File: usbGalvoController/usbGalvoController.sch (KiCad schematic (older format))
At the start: 26 parts, among them P1 USB_OTG, P2 CONN_01X06, P3 GND, P4 PWR, P5 DAC, P6 GPIO, P7 UART, U1 STM32L151x6, U2 LD1117S33CTR, Y1 8MHz

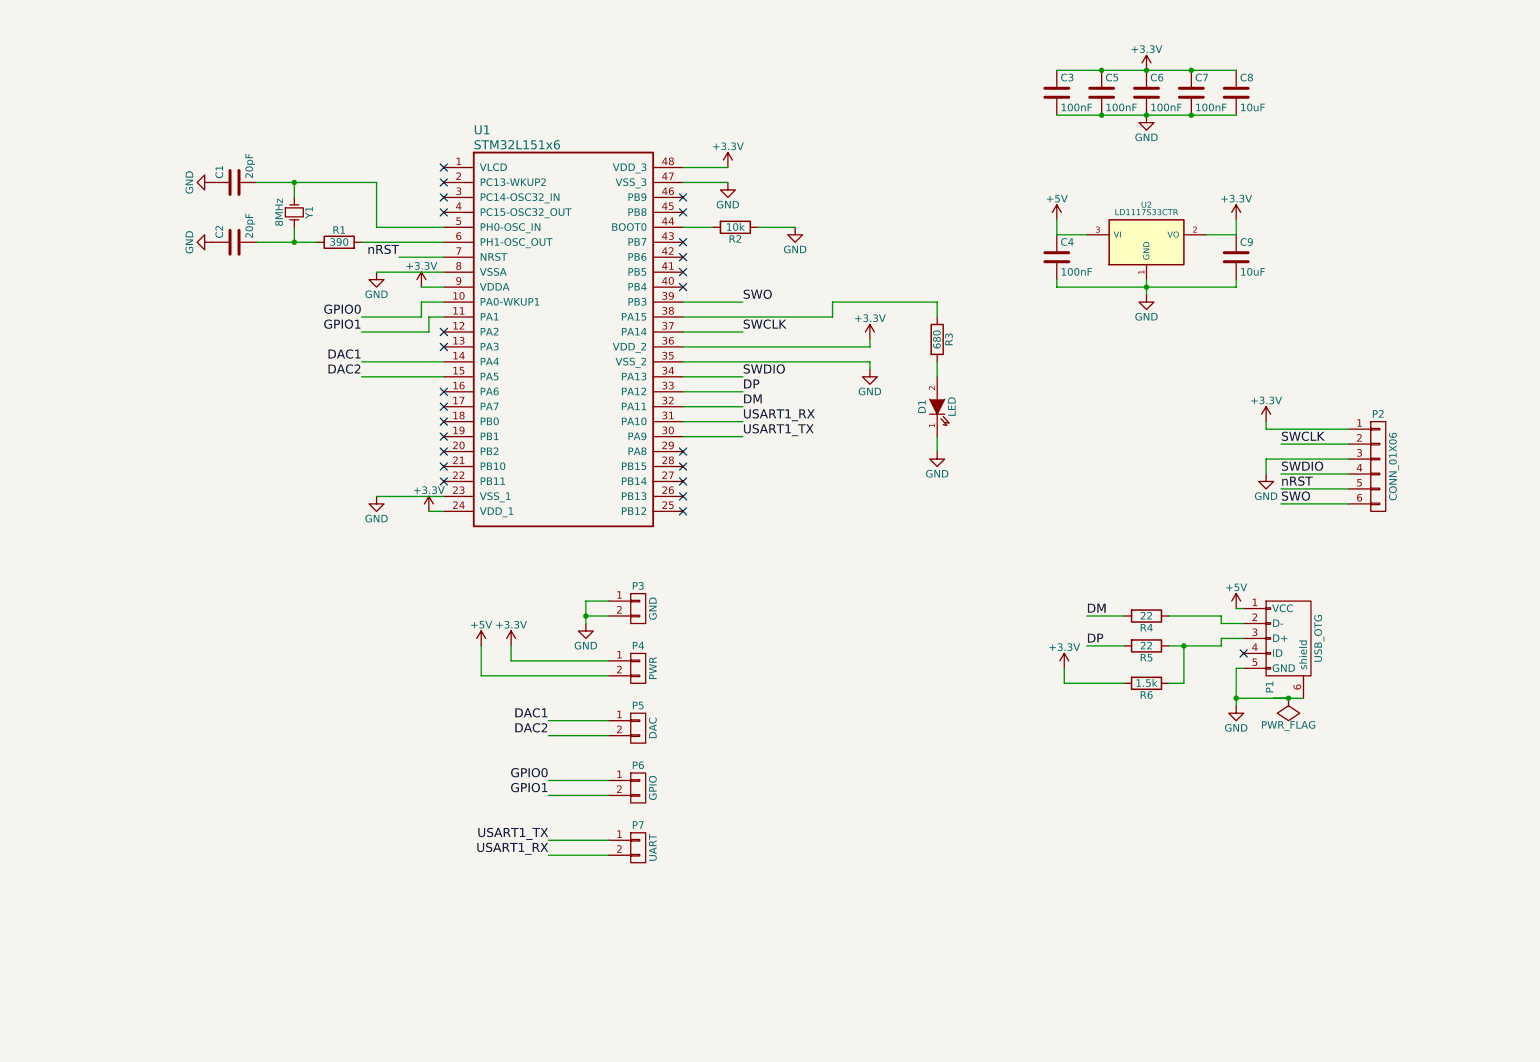
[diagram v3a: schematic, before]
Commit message: Start updating usbGalvoController schematic
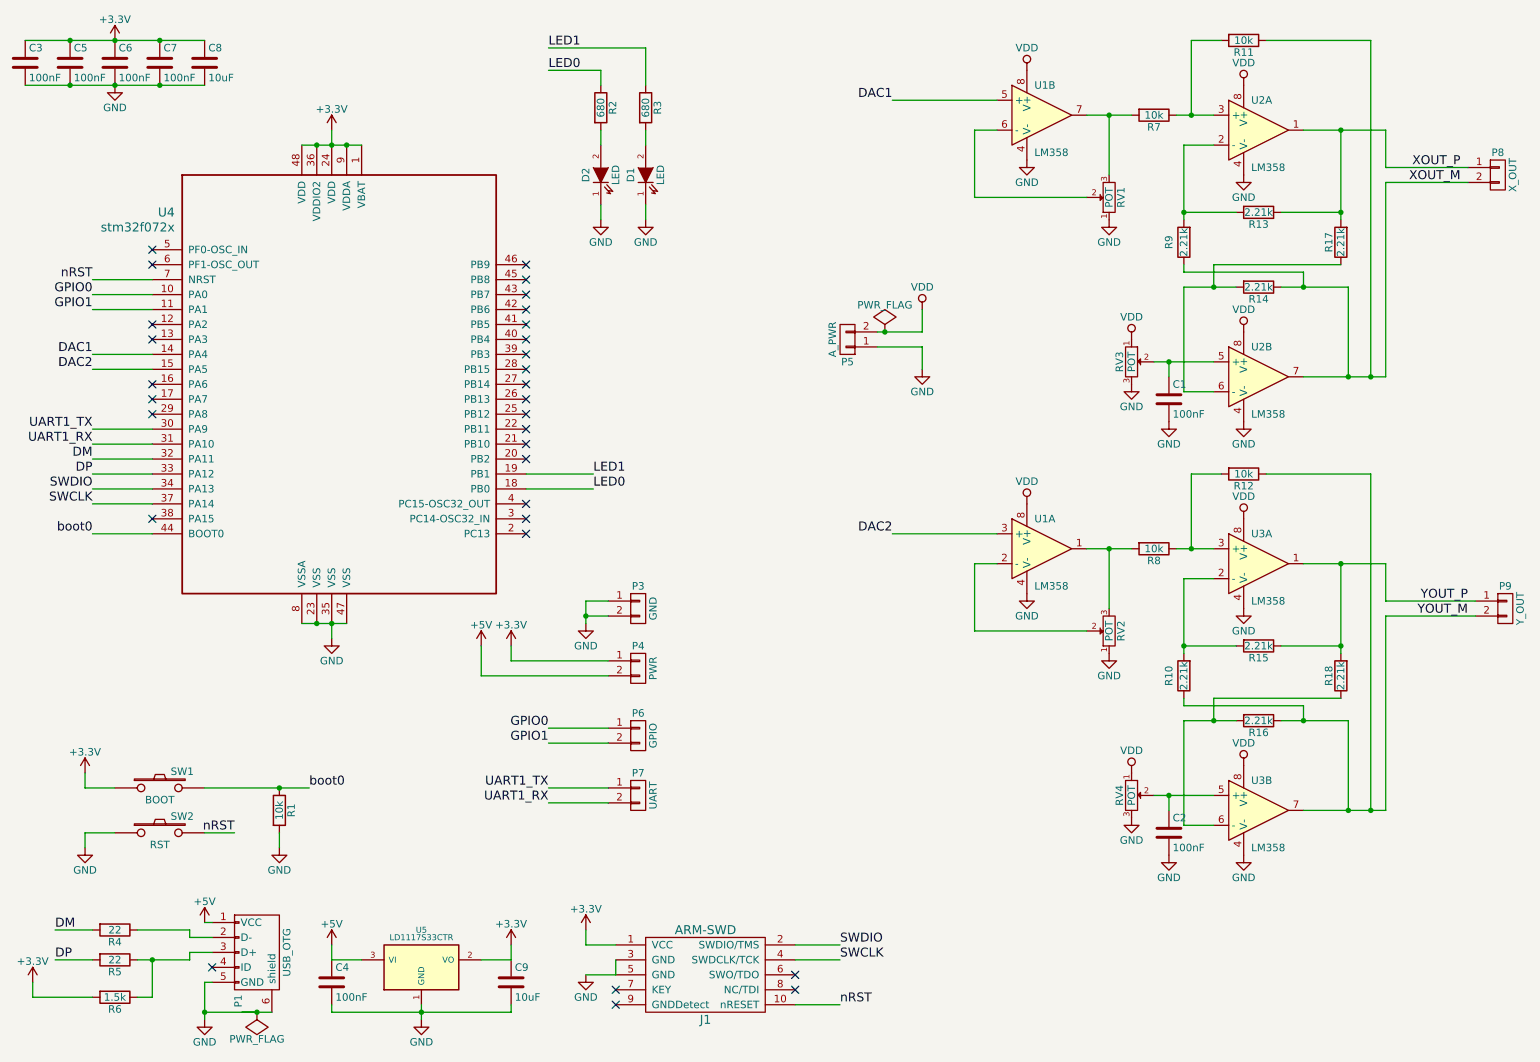
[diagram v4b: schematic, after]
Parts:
- removed P2: CONN_01X06, Pin_Headers:Pin_Header_Straight_1x06, symbol CONN_01X06
- removed U1: STM32L151x6, alvarop:LQFP48, symbol STM32L151x6
- removed Y1: 8MHz, symbol Crystal_Small
- added D2: LED, LEDs:LED-0805, symbol LED
- added J1: ARM-SWD, symbol ARM-SWD
- added P8: X_OUT, symbol CONN_01X02
- added P9: Y_OUT, symbol CONN_01X02
- added R10, R13, R14, R15, R16, R17, R18, R9: 2.21k, symbol R
- added R11, R12, R7, R8: 10k, symbol R
- added RV1, RV2, RV3, RV4: POT, symbol POT
- added SW1: BOOT, symbol SW_PUSH
- added SW2: RST, symbol SW_PUSH
- added U1, U2, U3: LM358, symbol LM358
- added U4: stm32f072x, symbol stm32f072x
- C1, C2: value 20pF -> 100nF
- P5: value DAC -> A_PWR; footprint Pin_Headers:Pin_Header_Straight_1x02 -> (none)
- R1: value 390 -> 10k
- R2: value 10k -> 680
- renumbered U2 to U5
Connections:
- net +3V3: now also J1.1 (VCC), SW1.1, U4.1 (VBAT), U4.24 (VDD), U4.36 (VDDIO2), U4.48 (VDD), U4.9 (VDDA)
- net DAC1: now also U1.5 (+), U4.14 (PA4); no longer P5.1 (P1)
- net DAC2: now also U1.3 (+), U4.15 (PA5); no longer P5.2 (P2)
- net DM: now also U4.32 (PA11)
- net DP: now also U4.33 (PA12)
- net GND: now also C1.2, C2.2, P5.1 (P1), R1.2, D2.1 (K), J1.3 (GND), J1.5 (GND), RV1.1, RV2.1, RV3.3, RV4.3, SW2.1, U1.4 (V-), U1.4 (V-), U2.4 (V-), U2.4 (V-), U3.4 (V-), U3.4 (V-), U4.23 (VSS), U4.35 (VSS), U4.47 (VSS), U4.8 (VSSA); no longer C1.1, C2.1, R2.1
- net GPIO0: now also U4.10 (PA0)
- net GPIO1: now also U4.11 (PA1)
- net SWCLK: now also J1.4 (SWDCLK/TCK), U4.37 (PA14)
- net SWDIO: now also J1.2 (SWDIO/TMS), U4.34 (PA13)
- net nRST: now also J1.10 (nRESET), SW2.2, U4.7 (NRST)
- net LED1: now reaches R3.1
- net LED1: now also U4.19 (PB1)
- net at R2.2: now also D2.2 (A)
- net boot0: now reaches R1.1
- net boot0: now also SW1.2, U4.44 (BOOT0); no longer C2.2
- net USART1_RX renamed UART1_RX
- net UART1_RX: now also U4.31 (PA10)
- net USART1_TX renamed UART1_TX
- net UART1_TX: now also U4.30 (PA9)
- new net: R13.2, R9.2, U2.2 (-)
- new net: R11.2, R7.1, U2.3 (+)
- new net: RV1.2, U1.6 (-)
- new net: R7.2, RV1.3, U1.7
- new net: C1.1, RV3.2, U2.5 (+)
- new net: R14.2, R17.1, U2.6 (-)
- new net: R10.2, R15.2, U3.2 (-)
- new net: R12.2, R8.1, U3.3 (+)
- new net: R8.2, RV2.3, U1.1
- new net: RV2.2, U1.2 (-)
- new net: C2.1, RV4.2, U3.5 (+)
- new net: R16.2, R18.1, U3.6 (-)
- new net LED0: R2.1, U4.18 (PB0)
- new net VDD: P5.2 (P2), RV3.1, RV4.1, U1.8 (V+), U1.8 (V+), U2.8 (V+), U2.8 (V+), U3.8 (V+), U3.8 (V+)
- new net XOUT_M: P8.2 (P2), R11.1, R14.1, R9.1, U2.7
- new net XOUT_P: P8.1 (P1), R13.1, R17.2, U2.1
- new net YOUT_M: P9.2 (P2), R10.1, R12.1, R16.1, U3.7
- new net YOUT_P: P9.1 (P1), R15.1, R18.2, U3.1
- no-connect marks 25 -> 30
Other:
- moved on the sheet: C3, C4, C5, C6, C7, C8, C9, D1, P1, P6, P7, R3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

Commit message: Finished layout for usbGalvoController v0.2
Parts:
- removed P7: UART, Pin_Headers:Pin_Header_Straight_1x02, symbol CONN_01X02
- added P2: CONN_01X06, Pin_Headers:Pin_Header_Straight_1x06, symbol CONN_01X06
- D1, D2: footprint LEDs:LED-0805 -> LEDs:LED_0805
- J1: footprint (none) -> footprints:ARM_SWD_SMD
- P5, P8, P9: footprint (none) -> Pin_Headers:Pin_Header_Straight_1x02
- R10, R11, R12, R13, R14, R15, R16, R17, R18, R7, R8, R9: footprint (none) -> Resistors_SMD:R_0805
- RV1, RV2, RV3, RV4: footprint (none) -> alvarop:POT-4mm
- SW1, SW2: footprint (none) -> footprints:PTS645SM43SMTR92
- U1, U2, U3: footprint (none) -> Housings_SOIC:SOIC-8_3.9x4.9mm_Pitch1.27mm
- U4: footprint (none) -> footprints:LQFP48
- U5: footprint alvarop:SOT-223 -> footprints:SOT-223
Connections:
- net +3V3: now also P2.3 (P3)
- net GND: now also P2.1 (P1)
- net GPIO0: now also P6.2 (P2), U4.16 (PA6); no longer P6.1 (P1), U4.10 (PA0)
- net GPIO1: now also P6.1 (P1), U4.17 (PA7); no longer P6.2 (P2), U4.11 (PA1)
- net UART1_RX: now also P2.5 (P5)
- net UART1_TX: now also P2.4 (P4)
- no-connect marks 30 -> 32

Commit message: Adding part numbers to usbGalvoController
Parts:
- C1, C2, C3, C4, C5, C6, C7: MPN (none) -> CL21F104ZBCNNNC
- C8, C9: MPN (none) -> CL21A106MQCLNNC
- D1, D2: MPN (none) -> LH R974-LP-1
- J1: MPN (none) -> 20021121-00010C4LF
- P1: MPN (none) -> 10118192-0001LF
- R1, R11, R12, R7, R8: MPN (none) -> RC2012J103CS
- R10, R13, R14, R15, R16, R17, R18, R9: MPN (none) -> RC2012J222CS
- R2, R3: MPN (none) -> RC2012J681CS
- R4, R5: MPN (none) -> RC2012J220CS
- R6: MPN (none) -> RC2012J152CS
- RV1, RV2, RV3, RV4: MPN (none) -> PVM4A104C01R00
- SW1, SW2: MPN (none) -> PTS645SM43SMTR92
- U1, U2, U3: MPN (none) -> LM358DR2G
- U4: MPN (none) -> STM32F072CBT6
- U5: MPN (none) -> LD1117S33CTR
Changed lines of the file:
@@
 F 2 "Capacitors_SMD:C_0805" H 1038 800 30  0001 C CNN
 F 3 "" H 1000 950 60  0000 C CNN
+F 4 "CL21F104ZBCNNNC" H 1000 950 60  0001 C CNN "MPN"
 	1    1000 950
 	1    0    0    -1
@@
 F 2 "Capacitors_SMD:C_0805" H 1638 800 30  0001 C CNN
 F 3 "" H 1600 950 60  0000 C CNN
+F 4 "CL21F104ZBCNNNC" H 1600 950 60  0001 C CNN "MPN"
 	1    1600 950
 	1    0    0    -1
@@
 F 2 "Capacitors_SMD:C_0805" H 1938 800 30  0001 C CNN
 F 3 "" H 1900 950 60  0000 C CNN
+F 4 "CL21F104ZBCNNNC" H 1900 950 60  0001 C CNN "MPN"
 	1    1900 950
 	1    0    0    -1
@@
 F 2 "Capacitors_SMD:C_0805" H 2238 800 30  0001 C CNN
 F 3 "" H 2200 950 60  0000 C CNN
+F 4 "CL21A106MQCLNNC" H 2200 950 60  0001 C CNN "MPN"
 	1    2200 950
 	1    0    0    -1
@@
 F 2 "Capacitors_SMD:C_0805" H 1338 800 30  0001 C CNN
 F 3 "" H 1300 950 60  0000 C CNN
+F 4 "CL21F104ZBCNNNC" H 1300 950 60  0001 C CNN "MPN"
 	1    1300 950
 	1    0    0    -1
@@
 F 2 "alvarop:USB_MICRO_B" V 2500 6800 60  0001 C CNN
 F 3 "" V 2500 6800 60  0000 C CNN
+F 4 "10118192-0001LF" H 2550 6900 60  0001 C CNN "MPN"
 	1    2550 6900
 	0    1    1    0
@@
 F 2 "Resistors_SMD:R_0805" V 1530 6750 30  0001 C CNN
 F 3 "" H 1600 6750 30  0000 C CNN
+F 4 "RC2012J220CS" V 1600 6750 60  0001 C CNN "MPN"
 	1    1600 6750
 	0    1    1    0
@@
 F 2 "Resistors_SMD:R_0805" V 1530 6950 30  0001 C CNN
 F 3 "" H 1600 6950 30  0000 C CNN
+F 4 "RC2012J220CS" V 1600 6950 60  0001 C CNN "MPN"
 	1    1600 6950
 	0    1    1    0
@@
 F 2 "footprints:SOT-223" H 3650 7100 40  0001 C CNN
 F 3 "" H 3650 7000 60  0000 C CNN
+F 4 "LD1117S33CTR" H 3650 7000 60  0001 C CNN "MPN"
 	1    3650 7000
 	1    0    0    -1
@@
 F 2 "Capacitors_SMD:C_0805" H 3088 6950 30  0001 C CNN
 F 3 "" H 3050 7100 60  0000 C CNN
+F 4 "CL21F104ZBCNNNC" H 3050 7100 60  0001 C CNN "MPN"
 	1    3050 7100
 	1    0    0    -1
@@
 F 2 "Capacitors_SMD:C_0805" H 4288 6950 30  0001 C CNN
 F 3 "" H 4250 7100 60  0000 C CNN
+F 4 "CL21A106MQCLNNC" H 4250 7100 60  0001 C CNN "MPN"
 	1    4250 7100
 	1    0    0    -1
@@
 F 2 "LEDs:LED_0805" H 5150 1700 60  0001 C CNN
 F 3 "" H 5150 1700 60  0000 C CNN
+F 4 "LH R974-LP-1" H 5150 1700 60  0001 C CNN "MPN"
 	1    5150 1700
 	0    -1   -1   0
@@
 F 2 "Resistors_SMD:R_0805" V 5080 1250 30  0001 C CNN
 F 3 "" H 5150 1250 30  0000 C CNN
+F 4 "RC2012J681CS" V 5150 1250 60  0001 C CNN "MPN"
 	1    5150 1250
 	1    0    0    -1
@@
 F 2 "Resistors_SMD:R_0805" V 1530 7200 30  0001 C CNN
 F 3 "" H 1600 7200 30  0000 C CNN
+F 4 "RC2012J152CS" V 1600 7200 60  0001 C CNN "MPN"
 	1    1600 7200
 	0    1    1    0
@@
 F 2 "footprints:LQFP48" H 1850 2200 60  0001 C CNN
 F 3 "" H 1850 2200 60  0000 C CNN
+F 4 "STM32F072CBT6" H 1850 2200 60  0001 C CNN "MPN"
 	1    1850 2200
 	1    0    0    -1
@@
 F 2 "LEDs:LED_0805" H 4850 1700 60  0001 C CNN
 F 3 "" H 4850 1700 60  0000 C CNN
+F 4 "LH R974-LP-1" H 4850 1700 60  0001 C CNN "MPN"
 	1    4850 1700
 	0    -1   -1   0
@@
 F 2 "Resistors_SMD:R_0805" V 4780 1250 30  0001 C CNN
 F 3 "" H 4850 1250 30  0000 C CNN
+F 4 "RC2012J681CS" V 4850 1250 60  0001 C CNN "MPN"
 	1    4850 1250
 	1    0    0    -1
@@
 F 2 "footprints:PTS645SM43SMTR92" H 1900 6100 50  0001 C CNN
 F 3 "" H 1900 6100 50  0000 C CNN
+F 4 "PTS645SM43SMTR92" H 1900 6100 60  0001 C CNN "MPN"
 	1    1900 6100
 	1    0    0    -1
@@
 F 2 "footprints:PTS645SM43SMTR92" H 1900 5800 50  0001 C CNN
 F 3 "" H 1900 5800 50  0000 C CNN
+F 4 "PTS645SM43SMTR92" H 1900 5800 60  0001 C CNN "MPN"
 	1    1900 5800
 	1    0    0    -1
@@
 F 2 "Resistors_SMD:R_0805" V 2630 5950 30  0001 C CNN
 F 3 "" H 2700 5950 30  0000 C CNN
+F 4 "RC2012J103CS" V 2700 5950 60  0001 C CNN "MPN"
 	1    2700 5950
 	1    0    0    -1
@@
 F 2 "Housings_SOIC:SOIC-8_3.9x4.9mm_Pitch1.27mm" H 9250 1400 50  0001 C CNN
 F 3 "" H 9250 1400 50  0000 C CNN
+F 4 "LM358DR2G" H 9250 1400 60  0001 C CNN "MPN"
 	1    9250 1400
 	1    0    0    -1
@@
 F 2 "Housings_SOIC:SOIC-8_3.9x4.9mm_Pitch1.27mm" H 7800 1300 50  0001 C CNN
 F 3 "" H 7800 1300 50  0000 C CNN
+F 4 "LM358DR2G" H 7800 1300 60  0001 C CNN "MPN"
 	2    7800 1300
 	1    0    0    -1
@@
 F 2 "alvarop:POT-4mm" H 8250 1850 50  0001 C CNN
 F 3 "" H 8250 1850 50  0000 C CNN
+F 4 "PVM4A104C01R00" H 8250 1850 60  0001 C CNN "MPN"
 	1    8250 1850
 	0    -1   -1   0
@@
 F 2 "alvarop:POT-4mm" H 8400 2950 50  0001 C CNN
 F 3 "" H 8400 2950 50  0000 C CNN
+F 4 "PVM4A104C01R00" H 8400 2950 60  0001 C CNN "MPN"
 	1    8400 2950
 	0    1    1    0
@@
 F 2 "Resistors_SMD:R_0805" V 8480 1300 50  0001 C CNN
 F 3 "" H 8550 1300 50  0000 C CNN
+F 4 "RC2012J103CS" V 8550 1300 60  0001 C CNN "MPN"
 	1    8550 1300
 	0    1    1    0
@@
 F 2 "Resistors_SMD:R_0805" V 9080 800 50  0001 C CNN
 F 3 "" H 9150 800 50  0000 C CNN
+F 4 "RC2012J103CS" V 9150 800 60  0001 C CNN "MPN"
 	1    9150 800
 	0    1    1    0
@@
 F 2 "Resistors_SMD:R_0805" V 9180 1950 50  0001 C CNN
 F 3 "" H 9250 1950 50  0000 C CNN
+F 4 "RC2012J222CS" V 9250 1950 60  0001 C CNN "MPN"
 	1    9250 1950
 	0    1    1    0
@@
 F 2 "Resistors_SMD:R_0805" V 9730 2150 50  0001 C CNN
 F 3 "" H 9800 2150 50  0000 C CNN
+F 4 "RC2012J222CS" V 9800 2150 60  0001 C CNN "MPN"
 	1    9800 2150
 	-1   0    0    1
@@
 F 2 "Resistors_SMD:R_0805" V 8680 2150 50  0001 C CNN
 F 3 "" H 8750 2150 50  0000 C CNN
+F 4 "RC2012J222CS" V 8750 2150 60  0001 C CNN "MPN"
 	1    8750 2150
 	-1   0    0    1
@@
 F 2 "Resistors_SMD:R_0805" V 9180 2450 50  0001 C CNN
 F 3 "" H 9250 2450 50  0000 C CNN
+F 4 "RC2012J222CS" V 9250 2450 60  0001 C CNN "MPN"
 	1    9250 2450
 	0    1    1    0
@@
 F 2 "Housings_SOIC:SOIC-8_3.9x4.9mm_Pitch1.27mm" H 9250 3050 50  0001 C CNN
 F 3 "" H 9250 3050 50  0000 C CNN
+F 4 "LM358DR2G" H 9250 3050 60  0001 C CNN "MPN"
 	2    9250 3050
 	1    0    0    -1
@@
 F 2 "Housings_SOIC:SOIC-8_3.9x4.9mm_Pitch1.27mm" H 9250 4300 50  0001 C CNN
 F 3 "" H 9250 4300 50  0000 C CNN
+F 4 "LM358DR2G" H 9250 4300 60  0001 C CNN "MPN"
 	1    9250 4300
 	1    0    0    -1
@@
 F 2 "Housings_SOIC:SOIC-8_3.9x4.9mm_Pitch1.27mm" H 7800 4200 50  0001 C CNN
 F 3 "" H 7800 4200 50  0000 C CNN
+F 4 "LM358DR2G" H 7800 4200 60  0001 C CNN "MPN"
 	1    7800 4200
 	1    0    0    -1
@@
 F 2 "alvarop:POT-4mm" H 8250 4750 50  0001 C CNN
 F 3 "" H 8250 4750 50  0000 C CNN
+F 4 "PVM4A104C01R00" H 8250 4750 60  0001 C CNN "MPN"
 	1    8250 4750
 	0    -1   -1   0
@@
 F 2 "alvarop:POT-4mm" H 8400 5850 50  0001 C CNN
 F 3 "" H 8400 5850 50  0000 C CNN
+F 4 "PVM4A104C01R00" H 8400 5850 60  0001 C CNN "MPN"
 	1    8400 5850
 	0    1    1    0
@@
 F 2 "Resistors_SMD:R_0805" V 8480 4200 50  0001 C CNN
 F 3 "" H 8550 4200 50  0000 C CNN
+F 4 "RC2012J103CS" V 8550 4200 60  0001 C CNN "MPN"
 	1    8550 4200
 	0    1    1    0
@@
 F 2 "Resistors_SMD:R_0805" V 9080 3700 50  0001 C CNN
 F 3 "" H 9150 3700 50  0000 C CNN
+F 4 "RC2012J103CS" V 9150 3700 60  0001 C CNN "MPN"
 	1    9150 3700
 	0    1    1    0
@@
 F 2 "Resistors_SMD:R_0805" V 9180 4850 50  0001 C CNN
 F 3 "" H 9250 4850 50  0000 C CNN
+F 4 "RC2012J222CS" V 9250 4850 60  0001 C CNN "MPN"
 	1    9250 4850
 	0    1    1    0
@@
 F 2 "Resistors_SMD:R_0805" V 9730 5050 50  0001 C CNN
 F 3 "" H 9800 5050 50  0000 C CNN
+F 4 "RC2012J222CS" V 9800 5050 60  0001 C CNN "MPN"
 	1    9800 5050
 	-1   0    0    1
@@
 F 2 "Resistors_SMD:R_0805" V 8680 5050 50  0001 C CNN
 F 3 "" H 8750 5050 50  0000 C CNN
+F 4 "RC2012J222CS" V 8750 5050 60  0001 C CNN "MPN"
 	1    8750 5050
 	-1   0    0    1
@@
 F 2 "Resistors_SMD:R_0805" V 9180 5350 50  0001 C CNN
 F 3 "" H 9250 5350 50  0000 C CNN
+F 4 "RC2012J222CS" V 9250 5350 60  0001 C CNN "MPN"
 	1    9250 5350
 	0    1    1    0
@@
 F 2 "Housings_SOIC:SOIC-8_3.9x4.9mm_Pitch1.27mm" H 9250 5950 50  0001 C CNN
 F 3 "" H 9250 5950 50  0000 C CNN
+F 4 "LM358DR2G" H 9250 5950 60  0001 C CNN "MPN"
 	2    9250 5950
 	1    0    0    -1
@@
 F 2 "Capacitors_SMD:C_0805" H 8688 3050 30  0001 C CNN
 F 3 "" H 8650 3200 60  0000 C CNN
+F 4 "CL21F104ZBCNNNC" H 8650 3200 60  0001 C CNN "MPN"
 	1    8650 3200
 	1    0    0    -1
@@
 F 2 "Capacitors_SMD:C_0805" H 8688 5950 30  0001 C CNN
 F 3 "" H 8650 6100 60  0000 C CNN
+F 4 "CL21F104ZBCNNNC" H 8650 6100 60  0001 C CNN "MPN"
 	1    8650 6100
 	1    0    0    -1
@@
 F 2 "footprints:ARM_SWD_SMD" H 5250 6900 60  0001 C CNN
 F 3 "" H 5250 6900 60  0000 C CNN
+F 4 "20021121-00010C4LF" H 5550 7050 60  0001 C CNN "MPN"
 	1    5550 7050
 	1    0    0    -1
